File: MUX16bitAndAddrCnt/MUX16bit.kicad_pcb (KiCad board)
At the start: 2 copper layers, 149.9 x 99.1 mm, 33 parts, among them J1 Conn_01x17_Female, J2 Conn_01x17_Female, J3 Conn_01x17_Female, J4 Conn_01x17_Female, J5 Conn_01x17_Female, J6 Conn_01x01_Male, J7 Conn_01x03_Male, J8 Screw_Terminal_01x02, J9 Conn_01x09_Male, Q1 IRLML5203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

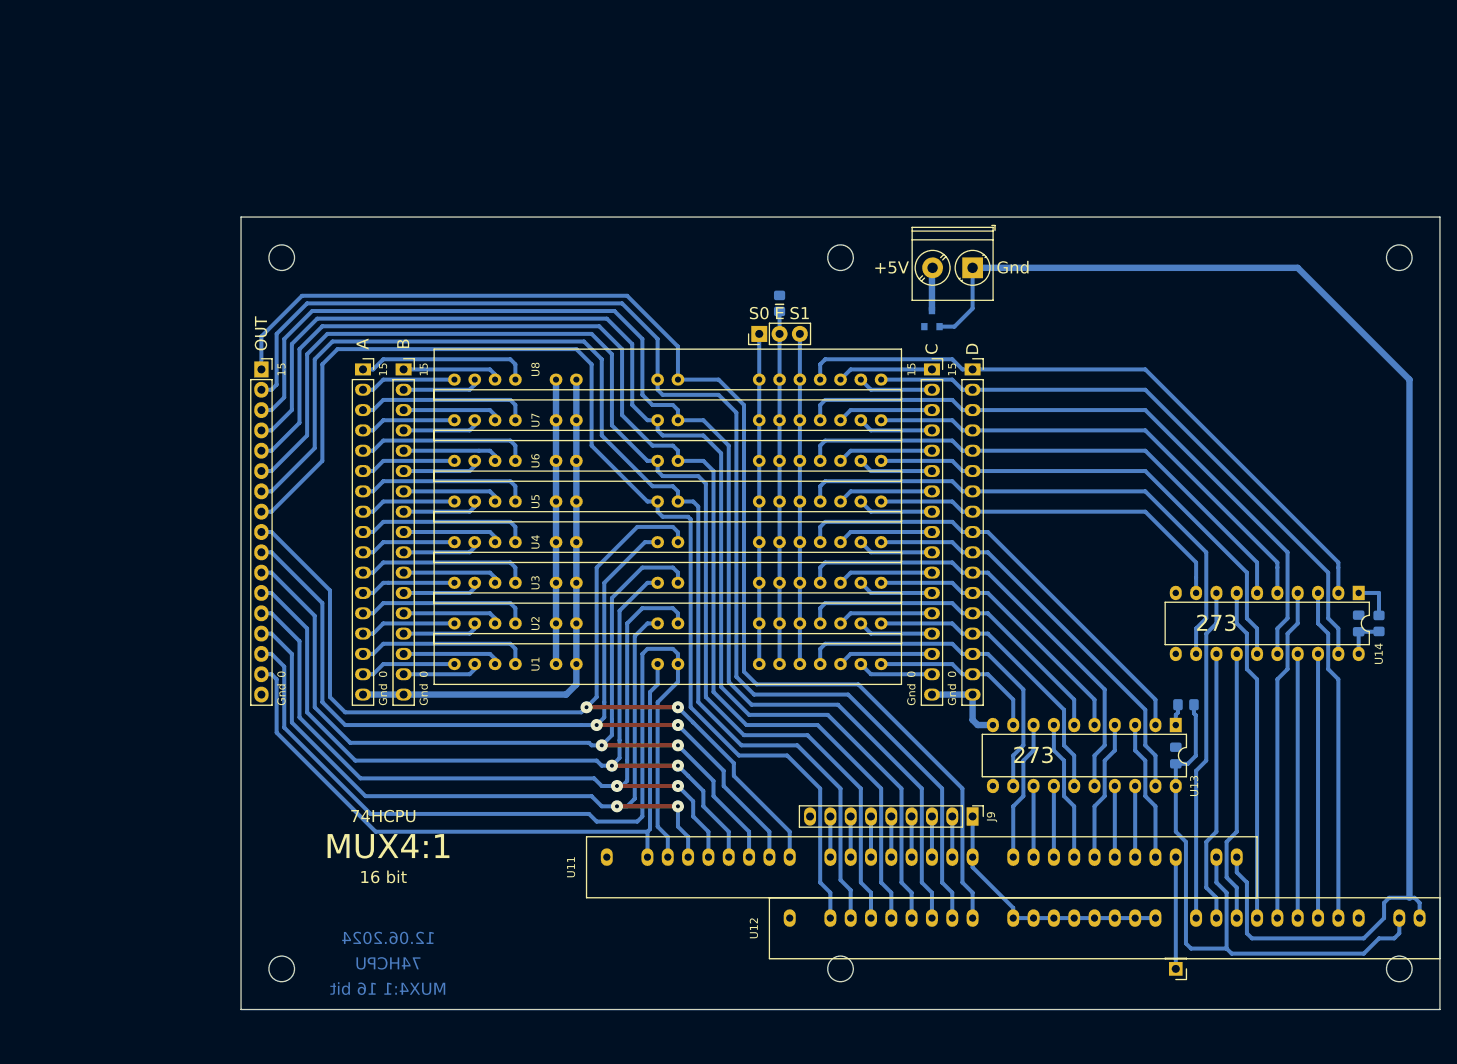
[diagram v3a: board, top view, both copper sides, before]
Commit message: Address counter in work
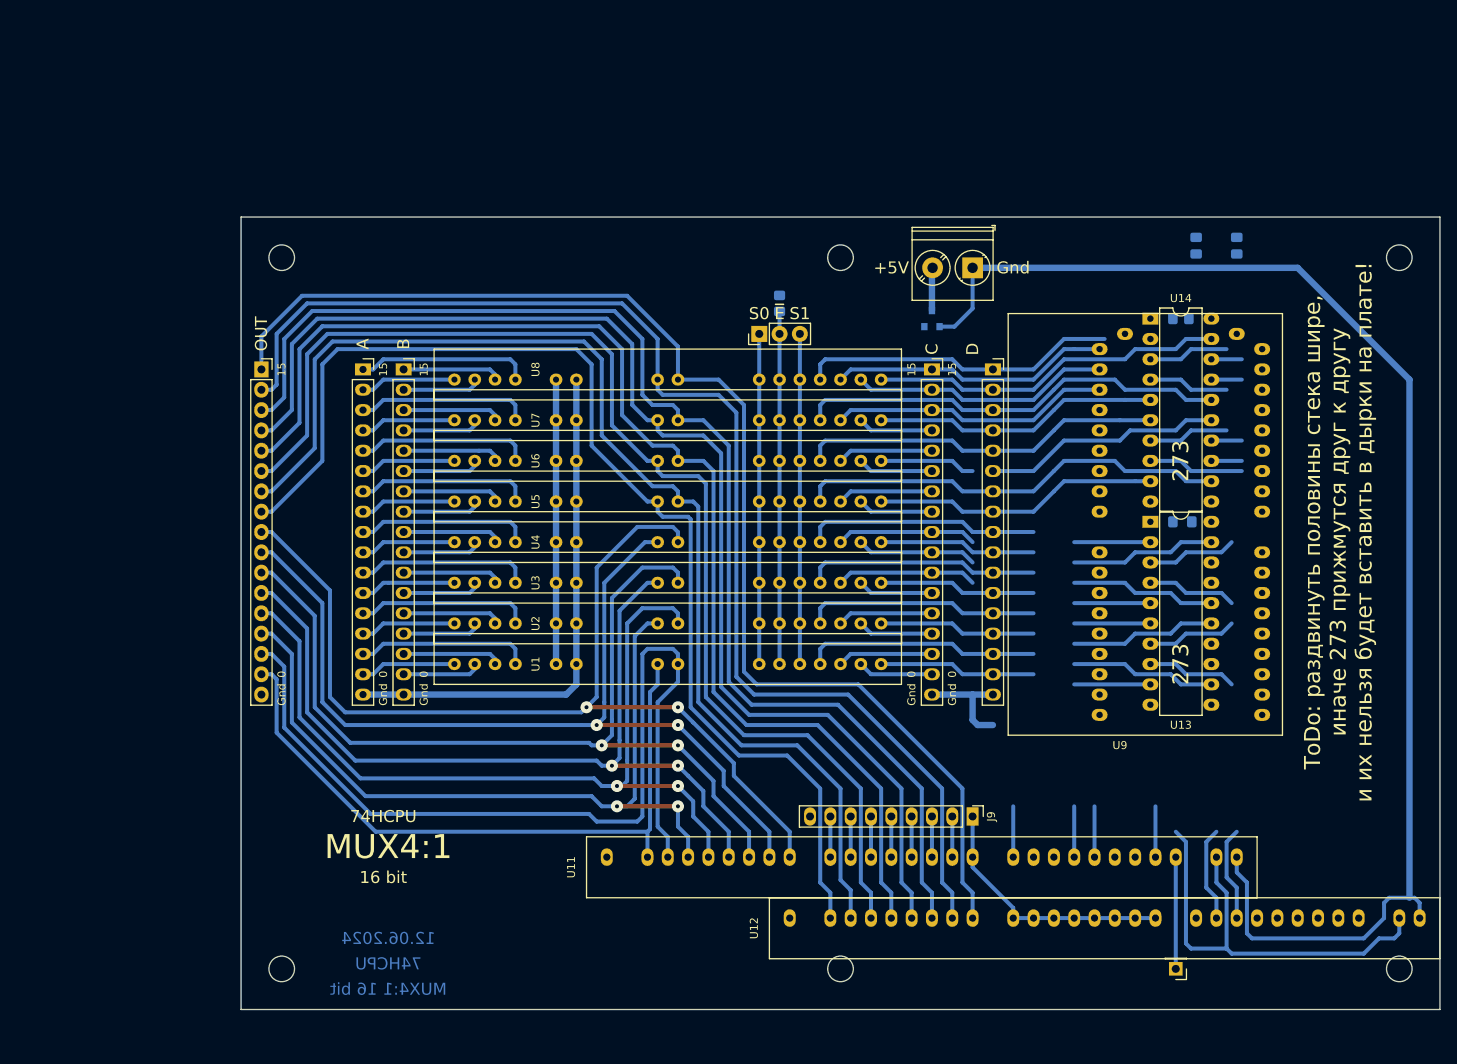
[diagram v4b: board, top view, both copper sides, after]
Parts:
- added U9: STACK16, CommonLibrary:STACK16, F.Cu at (140.3, 74.9)
- moved C1 64.2 mm to (137.2, 16.3)
- moved C2 51.4 mm to (132.1, 16.3)
- moved R2 45.4 mm to (130.2, 25.4), turned to 0 degrees
- moved U14 43.1 mm to (126.4, 25.4), turned to 0 degrees
- moved U13 25.6 mm to (126.4, 50.8), turned to 0 degrees
- moved R1 22.9 mm to (130.5, 50.8)
- moved J4 2.54 mm to (106.7, 31.8)
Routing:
- net /D15: track 81.3 -> 39.8 mm
- net /D14: track 76.6 -> 44.4 mm
- net /N15: track 41.7 -> 10.1 mm
- net /N12: track 41.7 -> 10.1 mm
- net /N11: track 41.7 -> 10.1 mm
- net /N8: track 41.7 -> 12.0 mm
- net /N14: track 33.0 -> 3.81 mm
- net /N13: track 33.0 -> 3.81 mm
- net /D13: track 81.7 -> 54.2 mm
- net /D12: track 60.7 -> 35.8 mm
- net VCC: track 115.4 -> 92.2 mm
- net /C15: track 12.0 -> 35.0 mm
- net /C14: track 9.42 -> 32.5 mm
- net /C13: track 12.0 -> 35.0 mm
- net /D11: track 66.9 -> 45.5 mm
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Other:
- board text added: "ToDo: раздвинуть половины стека шире, иначе 273 прижмутся друг к другу и их нельзя будет вставить в дырки на плате!"

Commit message: Address counter in work
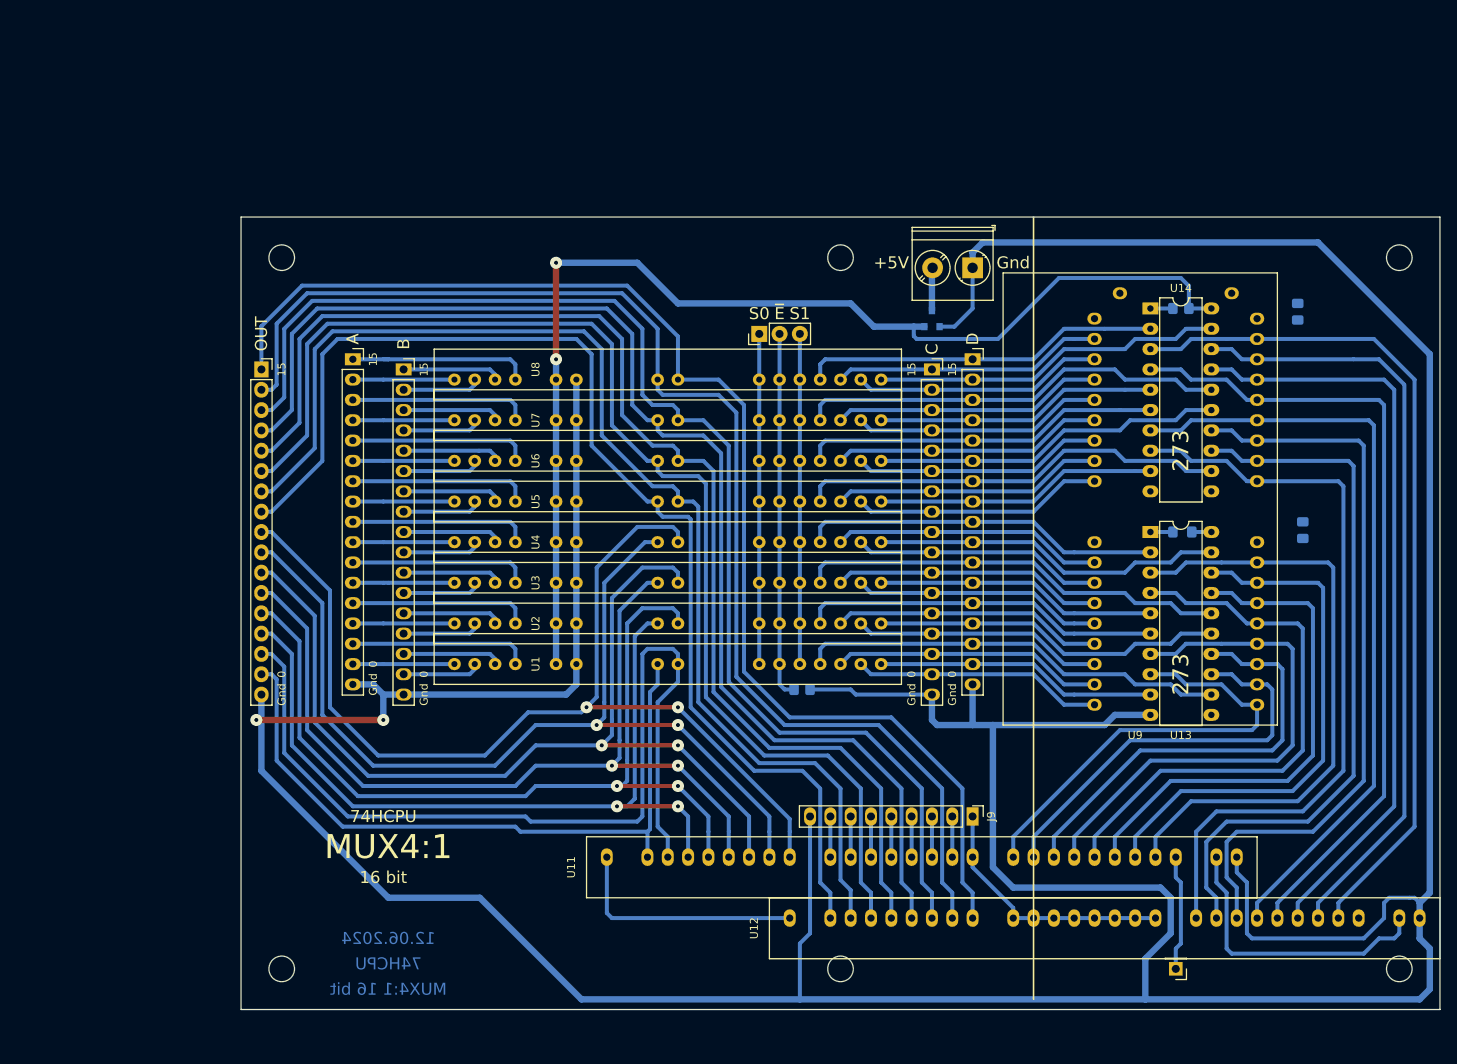
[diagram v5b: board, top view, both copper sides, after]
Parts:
- moved R3 48.3 mm to (82.8, 71.8), turned to 180 degrees
- moved C2 38.0 mm to (145.4, 51.8)
- moved C1 11.2 mm to (144.8, 24.5)
- moved J4 2.84 mm to (104.1, 30.5)
- moved J1 1.80 mm to (26.7, 30.5)
- moved U9 1.42 mm to (139.7, 73.7)
- moved R1 1.27 mm to (130.5, 52.1)
- moved U13 1.27 mm to (126.4, 52.1)
- moved R2 1.27 mm to (130.2, 24.1)
- moved U14 1.27 mm to (126.4, 24.1)
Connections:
- U9 pad 19: /C15 -> Net-(U9-Pad19)
- U9 pad 20: /C14 -> /C15
- U9 pad 21: /C13 -> /C14
- U9 pad 22: /C12 -> /C13
- U9 pad 23: /C11 -> /C12
- U9 pad 24: /C10 -> /C11
- U9 pad 25: /C9 -> /C10
- U9 pad 26: /C8 -> /C9
- U9 pad 27: Net-(U9-Pad27) -> /C8
- U9 pad 28: /C7 -> Net-(U9-Pad28)
- U9 pad 29: /C6 -> /C7
- U9 pad 30: /C5 -> /C6
- U9 pad 31: /C4 -> /C5
- U9 pad 32: /C3 -> /C4
- U9 pad 33: /C2 -> /C3
- U9 pad 34: /C1 -> /C2
- U9 pad 35: /C0 -> /C1
- U9 pad 36: Net-(U9-Pad36) -> /C0
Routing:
- net GND: track 251.5 -> 576.9 mm, vias 0 -> 2
- net /N15: track 10.1 -> 106.9 mm
- net /N14: track 3.81 -> 97.0 mm
- net VCC: track 92.2 -> 183.6 mm, vias 0 -> 2
- net /N13: track 3.81 -> 94.9 mm
- net /N12: track 10.1 -> 100.7 mm
- net /N11: track 10.1 -> 96.4 mm
- net /N8: track 12.0 -> 93.9 mm
- net /N10: track 15.7 -> 92.1 mm
- net /N9: track 15.7 -> 89.2 mm
- net /N6: track 0.00 -> 66.3 mm
- net /N5: track 0.63 -> 64.1 mm
- net /N7: track 17.6 -> 76.9 mm
- net /N2: track 0.00 -> 54.7 mm
- net /N1: track 0.00 -> 52.4 mm
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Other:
- board text removed: "ToDo: раздвинуть половины стека шире, иначе 273 прижмутся друг к другу и их нельзя будет вставить в дырки на плате!"

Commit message: Polishing Address counter
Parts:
- added J10: Conn_01x01_Male, Connector_PinHeader_2.54mm:PinHeader_1x01_P2.54mm_Vertical, F.Cu at (73.7, 100.3)
- added J11: Conn_01x01_Male, Connector_PinHeader_2.54mm:PinHeader_1x01_P2.54mm_Vertical, F.Cu at (139.7, 49.5)
- moved C2 93.1 mm to (53.4, 66.0), turned to 0 degrees
- moved C1 92.1 mm to (53.3, 35.6), turned to 0 degrees
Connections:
- U13 pad 11: Net-(U13-Pad11) -> /STEP
- U14 pad 11: Net-(U14-Pad11) -> /STEP
- U9 pad 18: Net-(U9-Pad18) -> GND
- U9 pad 19: Net-(U9-Pad19) -> VCC
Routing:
- net VCC: track 183.6 -> 262.8 mm, vias 2 -> 6
- net GND: track 576.9 -> 626.1 mm, vias 2 -> 4
- net /STEP: track 0.00 -> 42.3 mm, vias 0 -> 2
- net /N9: track 89.2 -> 91.2 mm
- net /N8: track 93.9 -> 95.5 mm
- net /+1\CNST: track 30.1 -> 29.0 mm
- net /O7: track 131.0 -> 130.0 mm
- net /O6: track 121.6 -> 120.5 mm
- net /O4: track 110.6 -> 109.5 mm
- net /O3: track 109.5 -> 108.4 mm
- net /O5: track 119.9 -> 118.9 mm
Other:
- board text added: "18.06.2024"
- board text added: "MUX4:1 & Address Counter"
- board text removed: "12.06.2024"
- board text removed: "MUX4:1"

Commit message: Polishing Address counter
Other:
- board text added: "+1/CONST"
- board text added: "19.06.2024"
- board text added: "7"
- board text added: "Addr Overflow"
- board text added: "CONST/ OFFSET"
- board text added: "STEP"
- board text removed: "18.06.2024"

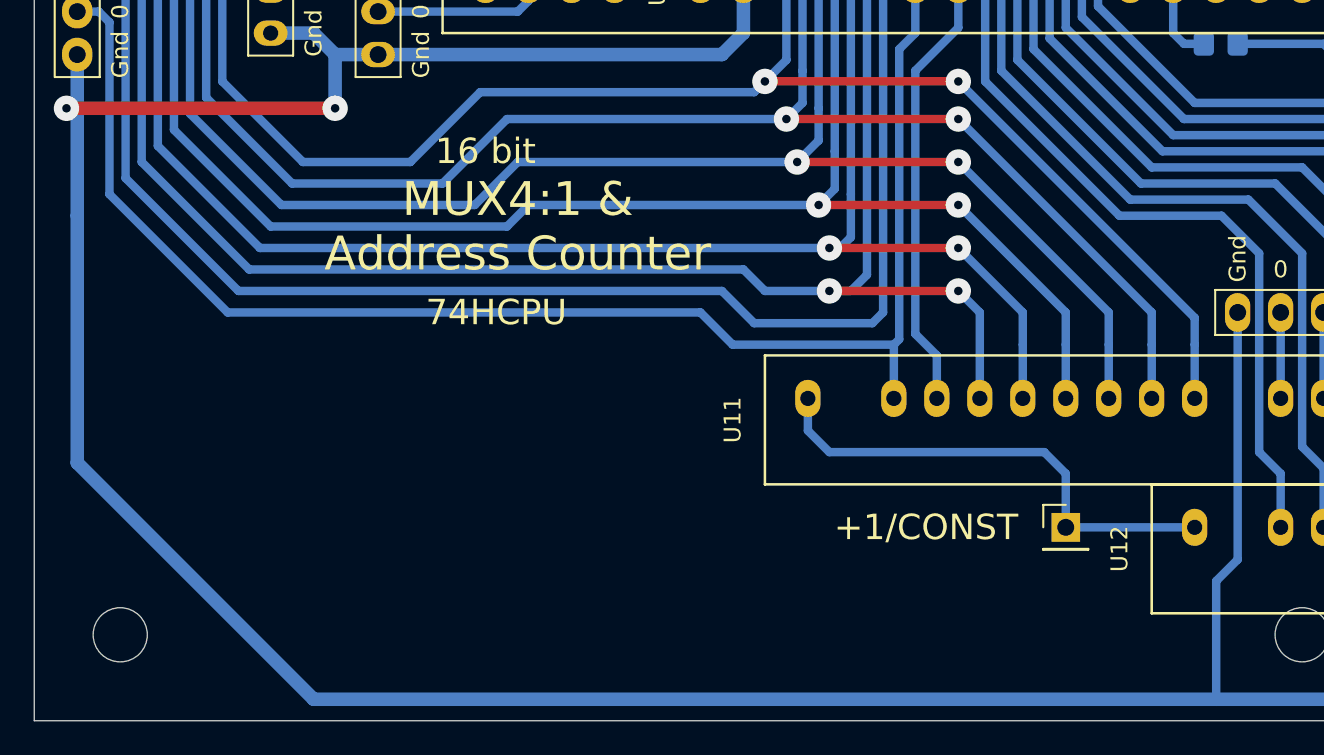
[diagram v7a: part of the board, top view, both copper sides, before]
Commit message: Address counter. Add gerbers. Remove stack counter.
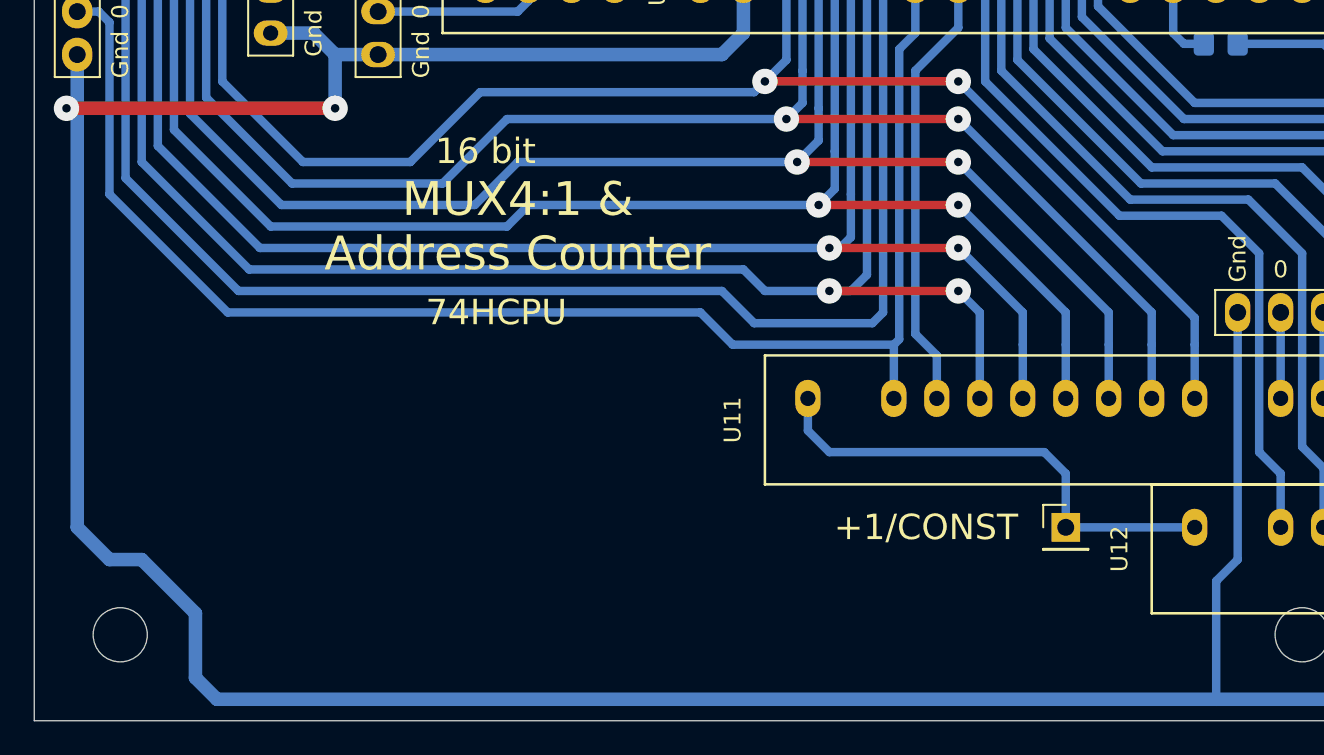
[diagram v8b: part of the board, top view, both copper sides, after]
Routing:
- net GND: track 626.1 -> 630.5 mm
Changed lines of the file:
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@@
     (thickness 1.6)
     (drawings 45)
-    (tracks 913)
+    (tracks 916)
     (zones 0)
     (modules 36)
@@
   (segment (start 105.41 15.875) (end 139.7 15.875) (width 0.8) (layer B.Cu) (net 65))
   (segment (start 139.7 15.875) (end 147.32 15.875) (width 0.8) (layer B.Cu) (net 65))
-  (segment (start 15.24 81.915) (end 15.24 75.565) (width 0.8) (layer B.Cu) (net 65))
-  (segment (start 15.24 96.52) (end 15.24 81.915) (width 0.8) (layer B.Cu) (net 65))
-  (segment (start 29.21 110.49) (end 15.24 96.52) (width 0.8) (layer B.Cu) (net 65))
-  (segment (start 82.55 110.49) (end 29.21 110.49) (width 0.8) (layer B.Cu) (net 65))
+  (segment (start 23.495 110.49) (end 82.55 110.49) (width 0.8) (layer B.Cu) (net 65))
+  (segment (start 22.225 109.22) (end 23.495 110.49) (width 0.8) (layer B.Cu) (net 65))
+  (segment (start 15.24 100.33) (end 17.145 102.235) (width 0.8) (layer B.Cu) (net 65))
+  (segment (start 15.24 75.565) (end 15.24 100.33) (width 0.8) (layer B.Cu) (net 65))
+  (segment (start 19.05 102.235) (end 22.225 105.41) (width 0.8) (layer B.Cu) (net 65))
+  (segment (start 22.225 105.41) (end 22.225 109.22) (width 0.8) (layer B.Cu) (net 65))
+  (segment (start 17.145 102.235) (end 19.05 102.235) (width 0.8) (layer B.Cu) (net 65))
   (segment (start 52.07 33.02) (end 52.07 68.58) (width 0.8) (layer B.Cu) (net 66))
   (segment (start 134.62 95.885) (end 134.62 92.71) (width 0.5) (layer B.Cu) (net 66))
